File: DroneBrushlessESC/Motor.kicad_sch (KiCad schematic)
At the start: 36 parts, among them Q91 CSD17577Q5A, Q92 CSD17577Q5A, Q93 CSD17577Q5A, Q94 CSD17577Q5A, Q95 CSD17577Q5A, Q96 CSD17577Q5A, U91 DRV8320SRTVR, U92 INA180A2, U93 INA180A2

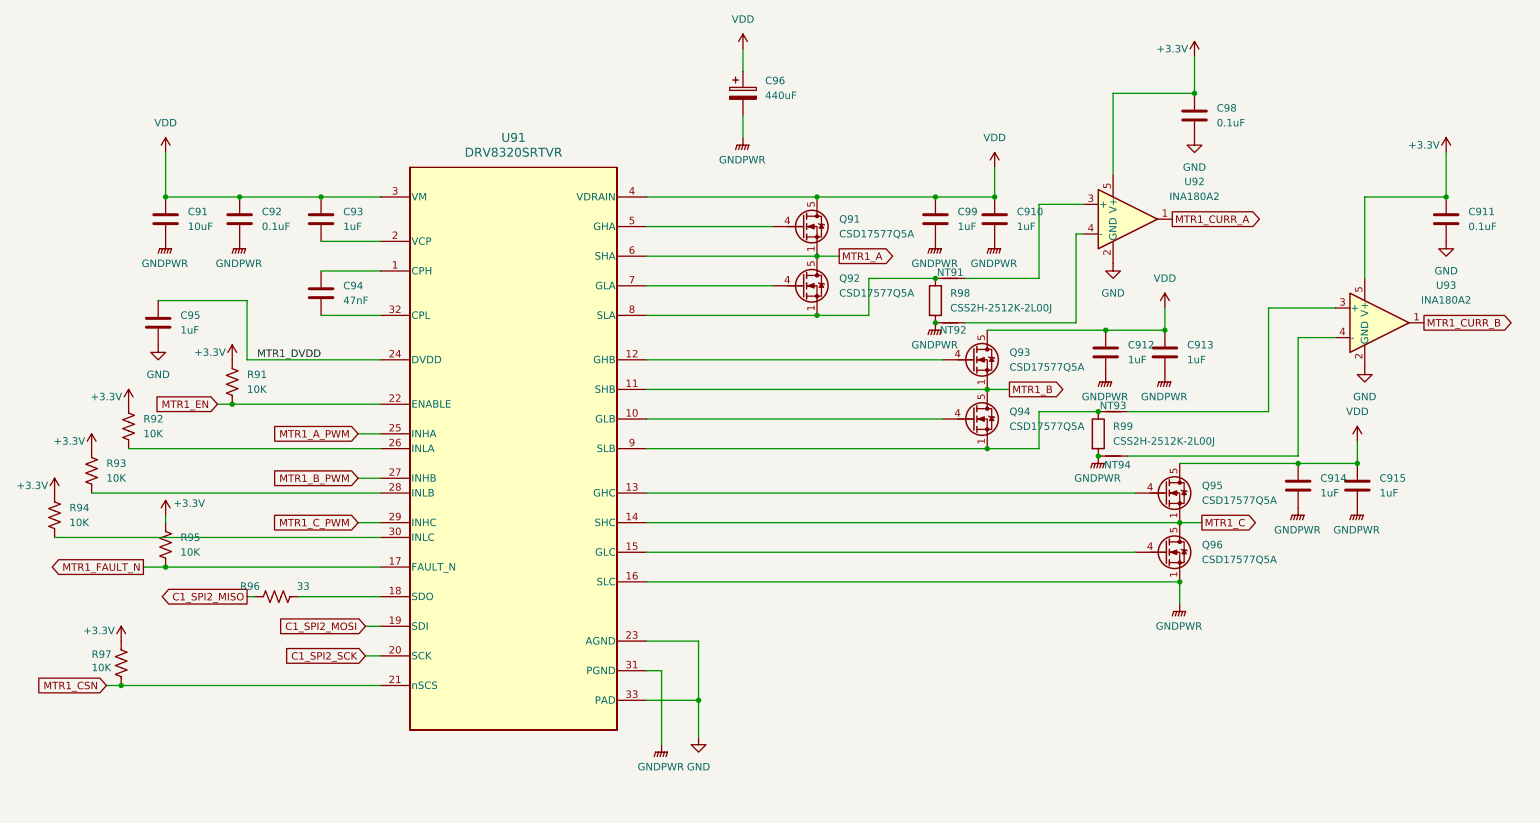
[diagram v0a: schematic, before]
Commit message: Completed schematic for brushless ESC and added needed components to main board.  The plan is to mount the ESCs on the main board using 2.54mm Vert Conn Headers
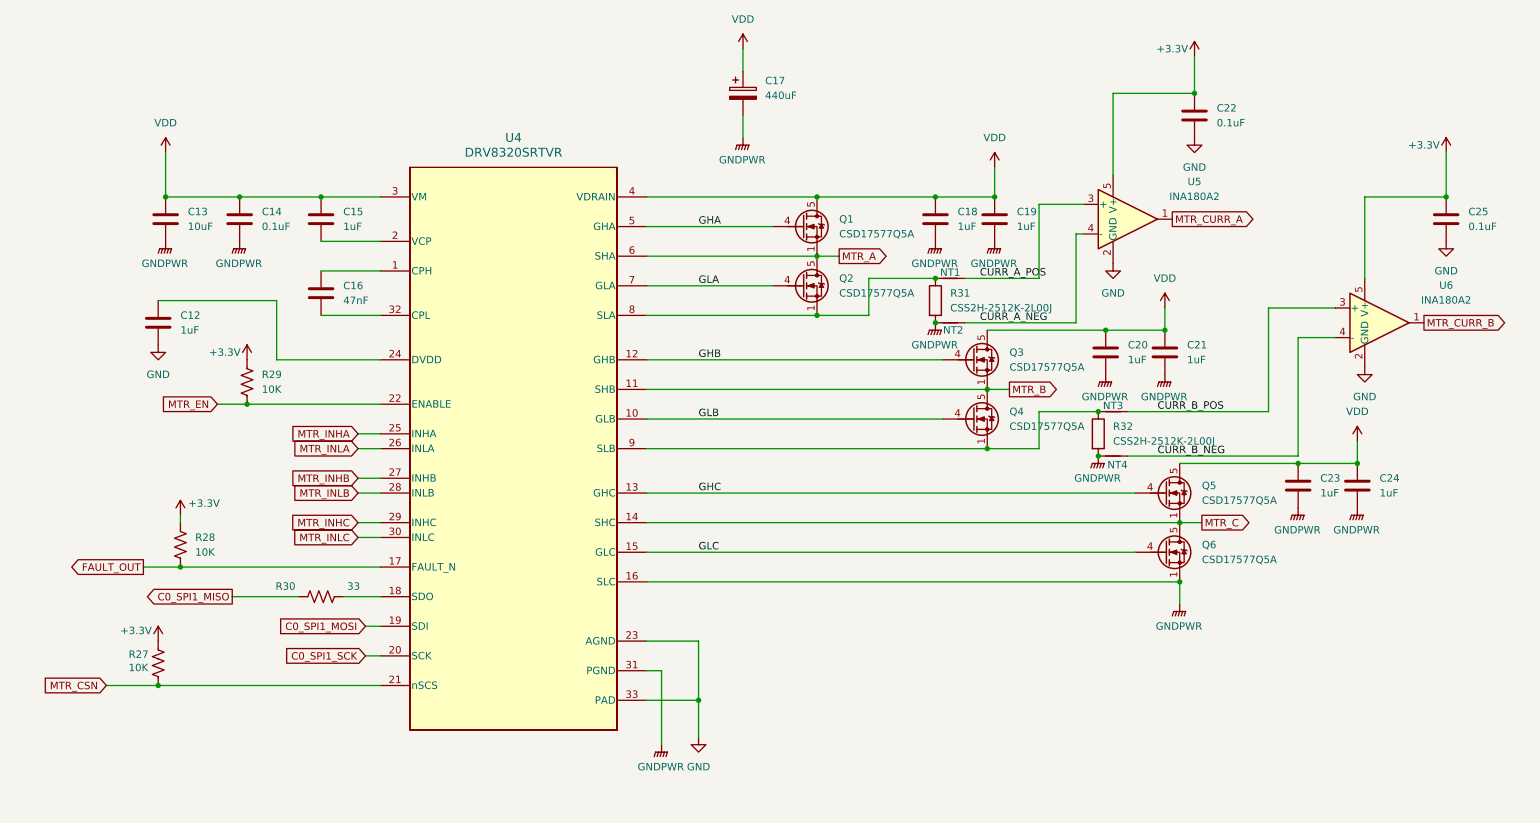
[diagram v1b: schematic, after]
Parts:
- removed R92, R93, R94: 10K, Resistor_SMD:R_0402_1005Metric, symbol Device:R_US
- removed R96: 33, Resistor_SMD:R_0402_1005Metric, symbol Device:R_US
- added R30: 33, Resistor_SMD:R_0402_1005Metric, symbol Device:R_US
- renumbered C95 to C12, C91 to C13, C92 to C14, C93 to C15, C94 to C16, C96 to C17, C99 to C18, C910 to C19, C912 to C20, C913 to C21, C98 to C22, C914 to C23, C915 to C24, C911 to C25, NT91 to NT1, NT92 to NT2, NT93 to NT3, NT94 to NT4, Q91 to Q1, Q92 to Q2, Q93 to Q3, Q94 to Q4, Q95 to Q5, Q96 to Q6, R97 to R27, R95 to R28, R91 to R29, R98 to R31, R99 to R32, U91 to U4, U92 to U5, U93 to U6
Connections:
- net CURR_B_POS: now reaches NT3.2, U6.3 (+)
- net CURR_B_NEG: now reaches NT4.2, U6.4 (-)
- net GLC: now reaches Q6.4 (G), U4.15 (GLC)
- net GLA: now reaches Q2.4 (G), U4.7 (GLA)
- net CURR_A_POS: now reaches NT1.2, U5.3 (+)
- net GHA: now reaches Q1.4 (G), U4.5 (GHA)
- net at U4.18 (SDO): now also R30.2
- net GLB: now reaches Q4.4 (G), U4.10 (GLB)
- net GHB: now reaches Q3.4 (G), U4.12 (GHB)
- net GHC: now reaches Q5.4 (G), U4.13 (GHC)
- net MTR_INLA: now reaches U4.26 (INLA)
- net MTR_INLB: now reaches U4.28 (INLB)
- net MTR_INLC: now reaches U4.30 (INLC)
- net CURR_A_NEG: now reaches NT2.2, U5.4 (-)
- net C1_SPI2_MOSI renamed C0_SPI1_MOSI
- net C1_SPI2_SCK renamed C0_SPI1_SCK
- net MTR1_A renamed MTR_A
- net MTR1_A_PWM renamed MTR_INHA
- net MTR1_B renamed MTR_B
- net MTR1_B_PWM renamed MTR_INHB
- net MTR1_C renamed MTR_C
- net MTR1_CSN renamed MTR_CSN
- net MTR1_CURR_A renamed MTR_CURR_A
- net MTR1_CURR_B renamed MTR_CURR_B
- net MTR1_C_PWM renamed MTR_INHC
- net MTR1_DVDD: no longer names the net of C12.1, U4.24 (DVDD)
- net MTR1_EN renamed MTR_EN
- net MTR1_FAULT_N renamed FAULT_OUT
- new net C0_SPI1_MISO: R30.1
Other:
- moved on the sheet: R27, R28, R29

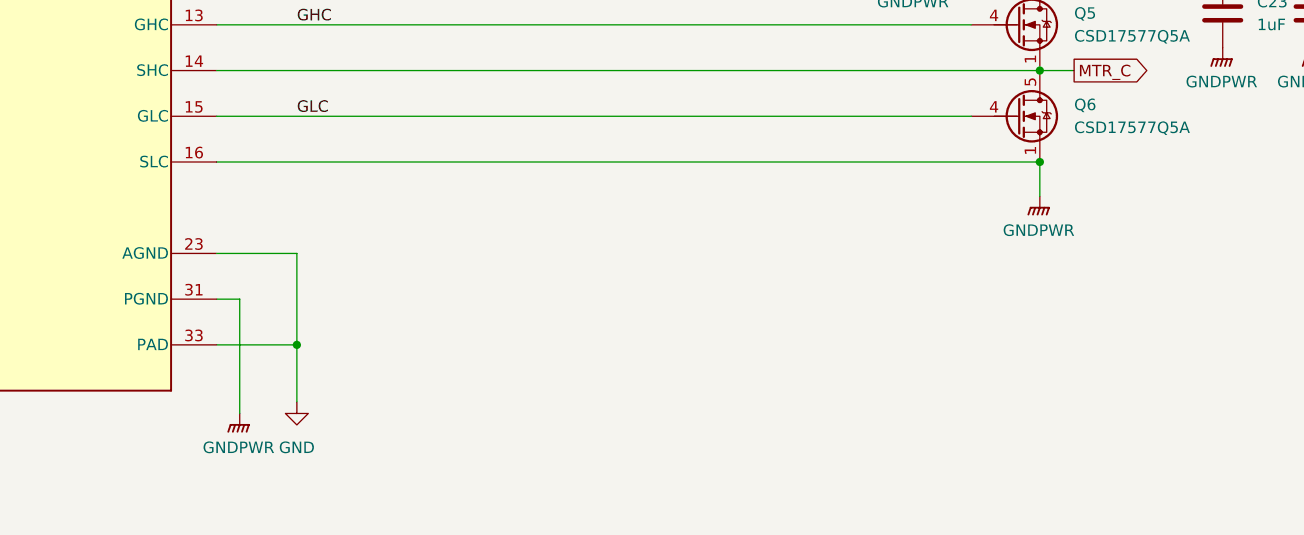
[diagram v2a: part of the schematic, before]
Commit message: Finished brushless driver layout
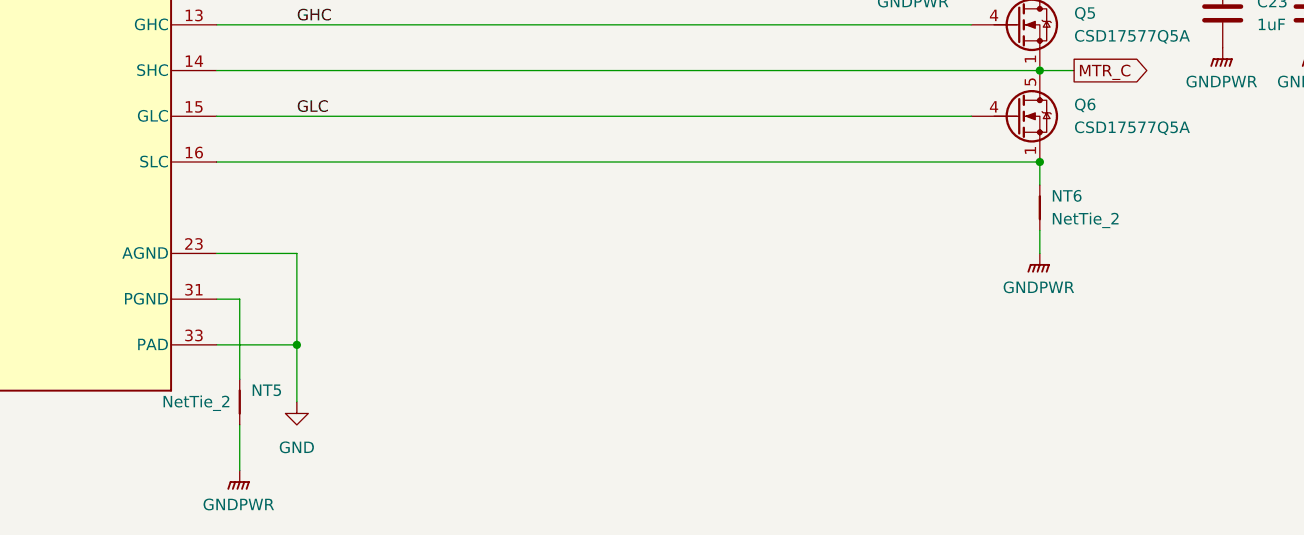
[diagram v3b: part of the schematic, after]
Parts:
- added NT5, NT6: NetTie_2, NetTie:NetTie-2_SMD_Pad0.5mm, symbol Device:NetTie_2
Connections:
- net GNDPWR: now also NT5.1, NT6.1; no longer Q6.1 (S), Q6.2 (S), Q6.3 (S), U4.16 (SLC), U4.31 (PGND)
- new net: NT6.2, Q6.1 (S), Q6.2 (S), Q6.3 (S), U4.16 (SLC)
- new net: NT5.2, U4.31 (PGND)
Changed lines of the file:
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@@
 	(wire
 		(pts
-			(xy 132.08 156.21) (xy 132.08 143.51)
+			(xy 132.08 162.56) (xy 132.08 157.48)
 		)
 		(stroke
@@
 	(wire
 		(pts
+			(xy 220.98 135.89) (xy 220.98 138.43)
+		)
+		(stroke
+			(width 0)
+			(type default)
+		)
+	)
+	(wire
+		(pts
 			(xy 80.01 105.41) (xy 83.82 105.41)
 		)
@@
 	(wire
 		(pts
+			(xy 132.08 152.4) (xy 132.08 143.51)
+		)
+		(stroke
+			(width 0)
+			(type default)
+		)
+	)
+	(wire
+		(pts
 			(xy 58.42 130.81) (xy 69.85 130.81)
 		)
@@
 	(wire
 		(pts
-			(xy 220.98 128.27) (xy 220.98 132.08)
+			(xy 80.01 113.03) (xy 83.82 113.03)
 		)
 		(stroke
@@
 	(wire
 		(pts
-			(xy 80.01 113.03) (xy 83.82 113.03)
+			(xy 241.3 106.68) (xy 241.3 86.36)
 		)
 		(stroke
@@
 	(wire
 		(pts
-			(xy 241.3 106.68) (xy 241.3 86.36)
+			(xy 179.07 76.2) (xy 167.64 76.2)
 		)
 		(stroke
@@
 	(wire
 		(pts
-			(xy 179.07 76.2) (xy 167.64 76.2)
+			(xy 146.05 36.83) (xy 146.05 40.64)
 		)
 		(stroke
@@
 	(wire
 		(pts
-			(xy 146.05 36.83) (xy 146.05 40.64)
+			(xy 196.85 76.2) (xy 196.85 63.5)
 		)
 		(stroke
@@
 	(wire
 		(pts
-			(xy 196.85 76.2) (xy 196.85 63.5)
+			(xy 187.96 95.25) (xy 191.77 95.25)
 		)
 		(stroke
@@
 	(wire
 		(pts
-			(xy 187.96 95.25) (xy 191.77 95.25)
+			(xy 220.98 128.27) (xy 220.98 130.81)
 		)
 		(stroke
@@
 	(symbol
 		(lib_id "power:GNDPWR")
-		(at 132.08 156.21 0)
+		(at 132.08 162.56 0)
 		(unit 1)
 		(exclude_from_sim no)
@@
 		(fields_autoplaced yes)
 		(property "Reference" "#PWR053"
-			(at 132.08 161.29 0)
+			(at 132.08 167.64 0)
 			(effects
 				(font
@@
 		)
 		(property "Value" "GNDPWR"
-			(at 131.953 160.02 0)
+			(at 131.953 166.37 0)
 			(effects
 				(font
@@
 		)
 		(property "Footprint" ""
-			(at 132.08 157.48 0)
+			(at 132.08 163.83 0)
 			(effects
 				(font
@@
 		)
 		(property "Datasheet" ""
-			(at 132.08 157.48 0)
+			(at 132.08 163.83 0)
 			(effects
 				(font
@@
 		)
 		(property "Description" "Power symbol creates a global label with name \"GNDPWR\" , global ground"
-			(at 132.08 156.21 0)
+			(at 132.08 162.56 0)
 			(effects
 				(font
@@
 	(symbol
 		(lib_id "power:GNDPWR")
-		(at 220.98 132.08 0)
+		(at 220.98 138.43 0)
 		(unit 1)
 		(exclude_from_sim no)
@@
 		(fields_autoplaced yes)
 		(property "Reference" "#PWR066"
-			(at 220.98 137.16 0)
+			(at 220.98 143.51 0)
 			(effects
 				(font
@@
 		)
 		(property "Value" "GNDPWR"
-			(at 220.853 135.89 0)
+			(at 220.853 142.24 0)
 			(effects
 				(font
@@
 		)
 		(property "Footprint" ""
-			(at 220.98 133.35 0)
+			(at 220.98 139.7 0)
 			(effects
 				(font
@@
 		)
 		(property "Datasheet" ""
-			(at 220.98 133.35 0)
+			(at 220.98 139.7 0)
 			(effects
 				(font
@@
 		)
 		(property "Description" "Power symbol creates a global label with name \"GNDPWR\" , global ground"
-			(at 220.98 132.08 0)
+			(at 220.98 138.43 0)
 			(effects
 				(font
@@
 	)
 	(symbol
+		(lib_id "Device:NetTie_2")
+		(at 132.08 154.94 90)
+		(unit 1)
+		(exclude_from_sim no)
+		(in_bom no)
+		(on_board yes)
+		(dnp no)
+		(property "Reference" "NT5"
+			(at 133.35 153.6699 90)
+			(effects
+				(font
+					(size 1.27 1.27)
+				)
+				(justify right)
+			)
+		)
+		(property "Value" "NetTie_2"
+			(at 123.444 154.94 90)
+			(effects
+				(font
+					(size 1.27 1.27)
+				)
+				(justify right)
+			)
+		)
+		(property "Footprint" "NetTie:NetTie-2_SMD_Pad0.5mm"
+			(at 132.08 154.94 0)
+			(effects
+				(font
+					(size 1.27 1.27)
+				)
+				(hide yes)
+			)
+		)
+		(property "Datasheet" "~"
+			(at 132.08 154.94 0)
+			(effects
+				(font
+					(size 1.27 1.27)
+				)
+				(hide yes)
+			)
+		)
+		(property "Description" "Net tie, 2 pins"
+			(at 132.08 154.94 0)
+			(effects
+				(font
+					(size 1.27 1.27)
+				)
+				(hide yes)
+			)
+		)
+		(pin "1"
+		)
+		(pin "2"
+		)
+		(instances
+			(project ""
+				(path "/3aa1a426-ad7e-4dd6-a1c5-7f97b630afc0/e65145b7-d6a3-4fa6-80d1-6d6a13317df0"
+					(reference "NT5")
+					(unit 1)
+				)
+			)
+		)
+	)
+	(symbol
 		(lib_id "power:GNDPWR")
 		(at 207.01 106.68 0)
@@
 					(unit 1)
 				)
+			)
+		)
+	)
+	(symbol
+		(lib_id "Device:NetTie_2")
+		(at 220.98 133.35 90)
+		(unit 1)
+		(exclude_from_sim no)
+		(in_bom no)
+		(on_board yes)
+		(dnp no)
+		(fields_autoplaced yes)
+		(property "Reference" "NT6"
+			(at 222.25 132.0799 90)
+			(effects
+				(font
+					(size 1.27 1.27)
+				)
+				(justify right)
+			)
+		)
+		(property "Value" "NetTie_2"
+			(at 222.25 134.6199 90)
+			(effects
+				(font
+					(size 1.27 1.27)
+				)
+				(justify right)
+			)
+		)
+		(property "Footprint" "NetTie:NetTie-2_SMD_Pad0.5mm"
+			(at 220.98 133.35 0)
+			(effects
+				(font
+					(size 1.27 1.27)
+				)
+				(hide yes)
+			)
+		)
+		(property "Datasheet" "~"
+			(at 220.98 133.35 0)
+			(effects
+				(font
+					(size 1.27 1.27)
+				)
+				(hide yes)
+			)
+		)
+		(property "Description" "Net tie, 2 pins"
+			(at 220.98 133.35 0)
+			(effects
+				(font
+					(size 1.27 1.27)
+				)
+				(hide yes)
+			)
+		)
+		(pin "2"
+		)
+		(pin "1"
+		)
+		(instances
+			(project ""
+				(path "/3aa1a426-ad7e-4dd6-a1c5-7f97b630afc0/e65145b7-d6a3-4fa6-80d1-6d6a13317df0"
+					(reference "NT6")
+					(unit 1)
+				)

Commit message: Finished Schematic for controller
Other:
- title: (none) -> Motor
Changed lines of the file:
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@@
 	(generator_version "9.0")
 	(paper "A4")
+	(title_block
+		(title "Motor")
+		(date "2026-02-23")
+		(rev "0-1")
+	)
 	(junction
 		(at 208.28 85.09)
